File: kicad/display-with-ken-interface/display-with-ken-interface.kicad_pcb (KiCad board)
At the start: 4 copper layers, 50.8 x 81.3 mm, 9 parts, among them J4 TFT_SPI, J5 Conn_01x08_Pin, U3 XDZ254-2-15-W-2.5-G1, U5 PM254-2-15-W-8.5

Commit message: add 3d models for display, adjust pin header placement
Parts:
- moved J5 65.7 mm to (74.9, 114.3), turned to 90 degrees
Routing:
- net GC9A01_RESET: track 63.6 -> 127.8 mm
- net GC9A01_BLK(Back light): track 150.2 -> 187.5 mm
- net GC9A01_CS: track 82.6 -> 51.1 mm, vias 1 -> 0
- net GC9A01_DC: track 55.1 -> 84.8 mm, vias 0 -> 1
- net GC9A01_SDA(MOSI): track 82.4 -> 109.7 mm
- net GC9A01_SCL: track 87.7 -> 107.9 mm
- net /IO13: track 80.8 -> 85.4 mm
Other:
- board text added: "1.69 TFT 240x280 1.8 TFT 128x160"
- board text added: "2.2 TFT 240x320"

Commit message: fix text
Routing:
- net GC9A01_BLK(Back light): track 187.5 -> 186.2 mm
- net TFT_CS: track 87.7 -> 86.9 mm
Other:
- board text added: "Display Extension Board with KEN Interface"
- board text removed: "Template for Extension board with EKN interface"

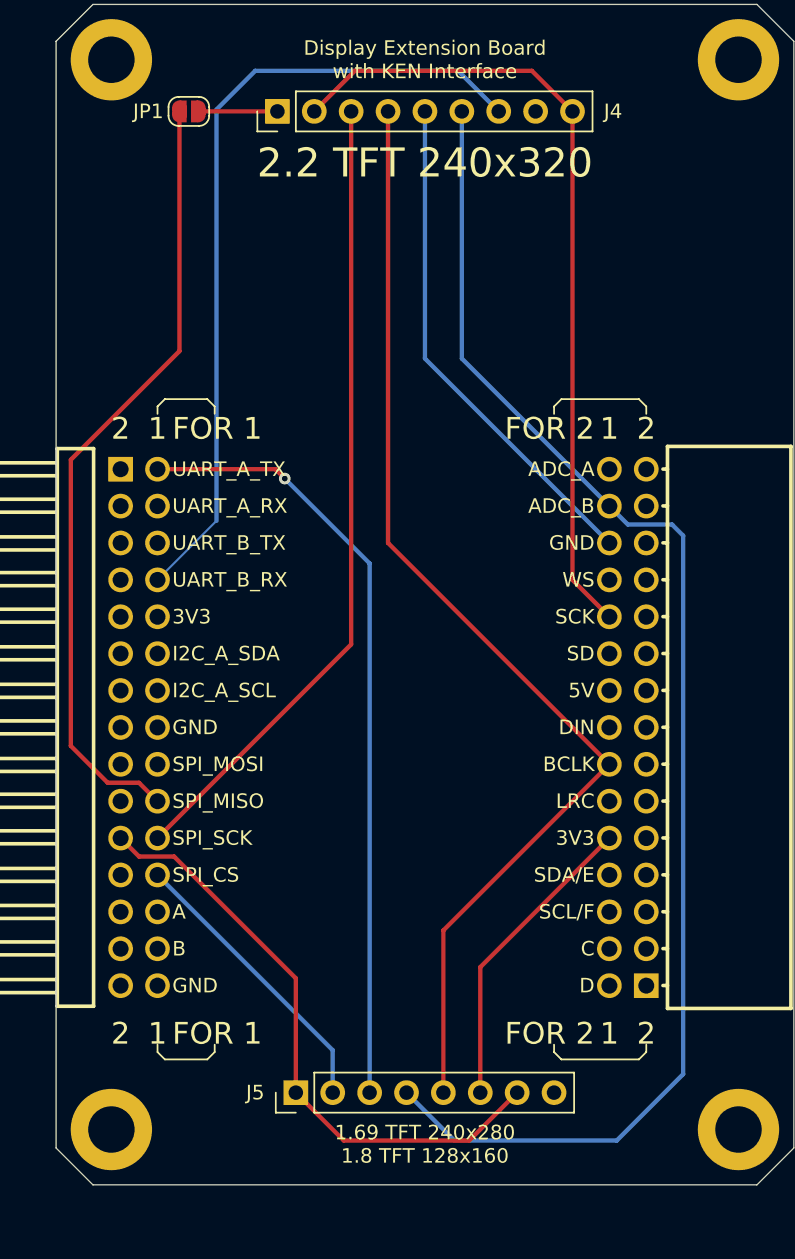
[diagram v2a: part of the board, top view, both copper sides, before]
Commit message: display board is ready to send to pcb maker
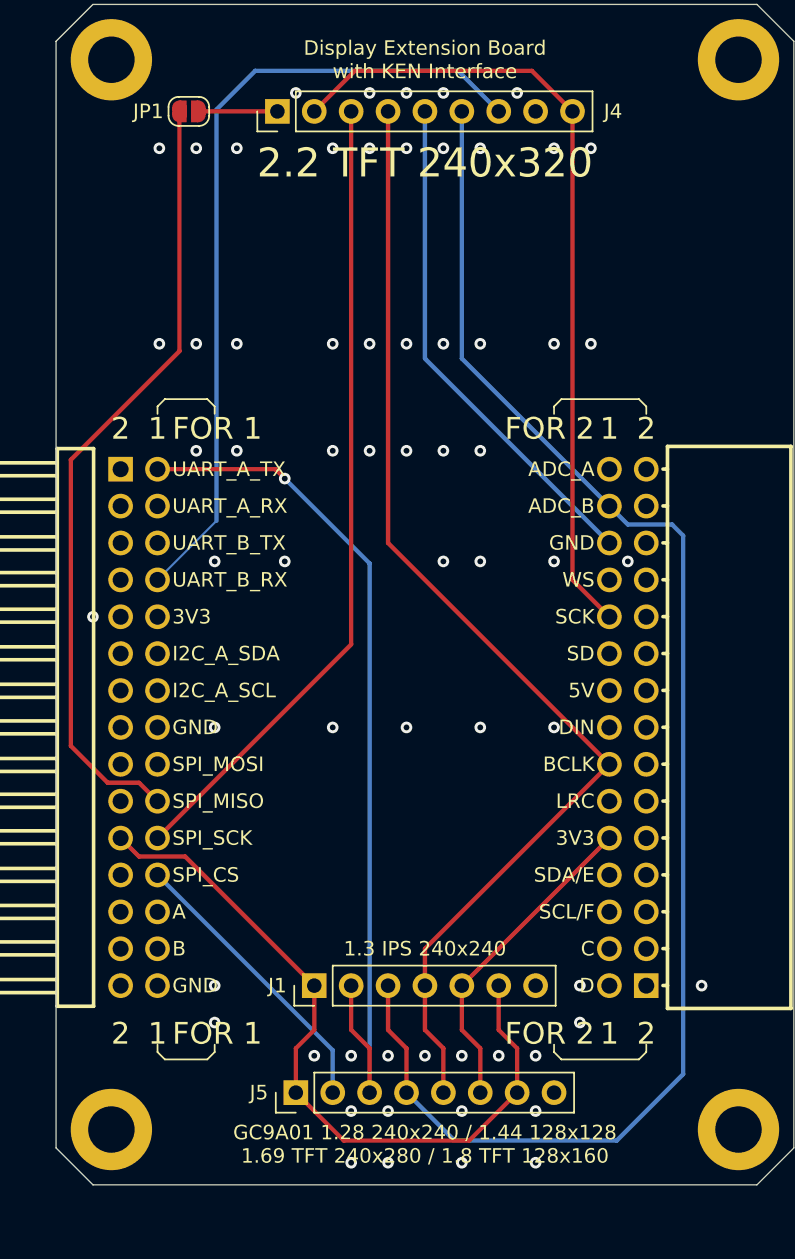
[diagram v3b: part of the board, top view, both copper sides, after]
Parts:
- added J1: Conn_01x07_Pin, Connector_PinHeader_2.54mm:PinHeader_1x07_P2.54mm_Vertical, F.Cu at (76.2, 106.9)
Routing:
- net GC9A01_BLK(Back light): track 186.2 -> 195.6 mm
- net GC9A01_DC: track 84.8 -> 92.7 mm
- net GC9A01_RESET: track 127.8 -> 135.7 mm
- net GC9A01_SDA(MOSI): track 109.7 -> 110.8 mm
- net GC9A01_SCL: track 107.9 -> 108.9 mm
- net FTF_GND: vias 0 -> 64
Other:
- board text added: "1.3 IPS 240x240"
- board text added: "GC9A01 1.28 240x240 / 1.44 128x128 1.69 TFT 240x280 / 1.8 TFT 128x160"
- board text added: "version:1.0 date: 20260224"
- board text removed: "1.69 TFT 240x280 1.8 TFT 128x160"
- board text removed: "version:1.0 date: 20260202"

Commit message: update symbol
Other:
- board text added: "CS for large"
- board text added: "DC for large"
- board text added: "DC for small"
- board text added: "RESET"
